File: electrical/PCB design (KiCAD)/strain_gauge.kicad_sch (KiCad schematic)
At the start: 12 parts, among them U6 INA125U

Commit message: documentation update for my 10 days leave ; documentation for first time teensy setup on Arduino IDE ;  SW revamp to use HW versioning conditional compiling
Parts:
- added R19, R23: 1M, Resistor_THT:R_Axial_DIN0207_L6.3mm_D2.5mm_P10.16mm_Horizontal, symbol TMotor_Rev0_5_1_Mark_2_NAU_OpenExo-eagle-import:R-US_0207/10
- R16: value 470R -> 10R
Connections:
- net GND: now also R19.2, R23.2
- net Vbridge+: now also R19.1
- net Vbridge-: now also R23.1
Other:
- note added: "weak pull down to avoid saturating output amplifier"

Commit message: design updates ; documentation update
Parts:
- removed C19: 100nF, Capacitor_THT:C_Disc_D10.5mm_W5.0mm_P5.00mm, symbol TMotor_Rev0_5_1_Mark_2_NAU_OpenExo-eagle-import:C-EU050-024X044
- removed D1: BAT54S, Package_TO_SOT_SMD:SOT-23, symbol Diode:BAT54S
- removed INA_EXC_JP6: SolderJumper_3_Open, Jumper:SolderJumper-3_P1.3mm_Open_RoundedPad1.0x1.5mm_NumberLabels, symbol Jumper:SolderJumper_3_Open
- added C32, C36: 10nF, Capacitor_SMD:C_0805_2012Metric_Pad1.18x1.45mm_HandSolder, symbol TMotor_Rev0_5_1_Mark_2_NAU_OpenExo-eagle-import:C-EU050-024X044
- added D7: BAS70-04, BAS70-04:P200_SOT-23, symbol BAS70-04:BAS70-04
- added INA_EXC_JP2: SolderJumper_2_Open, Jumper:SolderJumper-2_P1.3mm_Open_RoundedPad1.0x1.5mm, symbol Jumper:SolderJumper_2_Open
- added R22: 1k, Resistor_SMD:R_0805_2012Metric_Pad1.20x1.40mm_HandSolder, symbol Device:R
- C13: renamed from C10; footprint (none) -> Capacitor_SMD:C_0805_2012Metric_Pad1.18x1.45mm_HandSolder
- C14: renamed from C24; footprint Capacitor_THT:C_Disc_D10.5mm_W5.0mm_P5.00mm -> Capacitor_SMD:C_0805_2012Metric_Pad1.18x1.45mm_HandSolder
- C15: renamed from C14; footprint (none) -> Capacitor_SMD:C_0805_2012Metric_Pad1.18x1.45mm_HandSolder
- C16: renamed from C25; footprint Capacitor_THT:C_Disc_D10.5mm_W5.0mm_P5.00mm -> Capacitor_SMD:C_0805_2012Metric_Pad1.18x1.45mm_HandSolder
- R6: renamed from R3; value 4.7k -> 1k; footprint Resistor_THT:R_Axial_DIN0207_L6.3mm_D2.5mm_P10.16mm_Horizontal -> Resistor_SMD:R_0805_2012Metric_Pad1.20x1.40mm_HandSolder
- R7: renamed from R16; value 10R -> 50; footprint Resistor_THT:R_Axial_DIN0207_L6.3mm_D2.5mm_P10.16mm_Horizontal -> Resistor_SMD:R_0805_2012Metric_Pad1.20x1.40mm_HandSolder
- R8: renamed from R19; value 1M -> 100k; footprint Resistor_THT:R_Axial_DIN0207_L6.3mm_D2.5mm_P10.16mm_Horizontal -> Resistor_SMD:R_0805_2012Metric_Pad1.20x1.40mm_HandSolder
- R9: renamed from R23; value 1M -> 100k; footprint Resistor_THT:R_Axial_DIN0207_L6.3mm_D2.5mm_P10.16mm_Horizontal -> Resistor_SMD:R_0805_2012Metric_Pad1.20x1.40mm_HandSolder
- renumbered INA_PWR_JP6 to INA_PWR_JP2, INA_VREF_JP6 to INA_VREF_JP2, U6 to U2
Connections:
- net +3V3: now also D7.2 (C)
- net GND: now also C32.1, C36.1, D7.1 (A)
- net Vamplified: now also C32.2, D7.3
- net Vexcitation+: now also C36.2, R22.2
- net at INA_VREF_JP2.2 (C), U2.4 (VREFOUT), U2.5 (IAREF): now also INA_EXC_JP2.1 (A)
- new net: INA_EXC_JP2.2 (B), R22.1
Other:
- note added: "ADC kickback filter for Nano's sample and hold current transients"
- moved on the sheet: R9

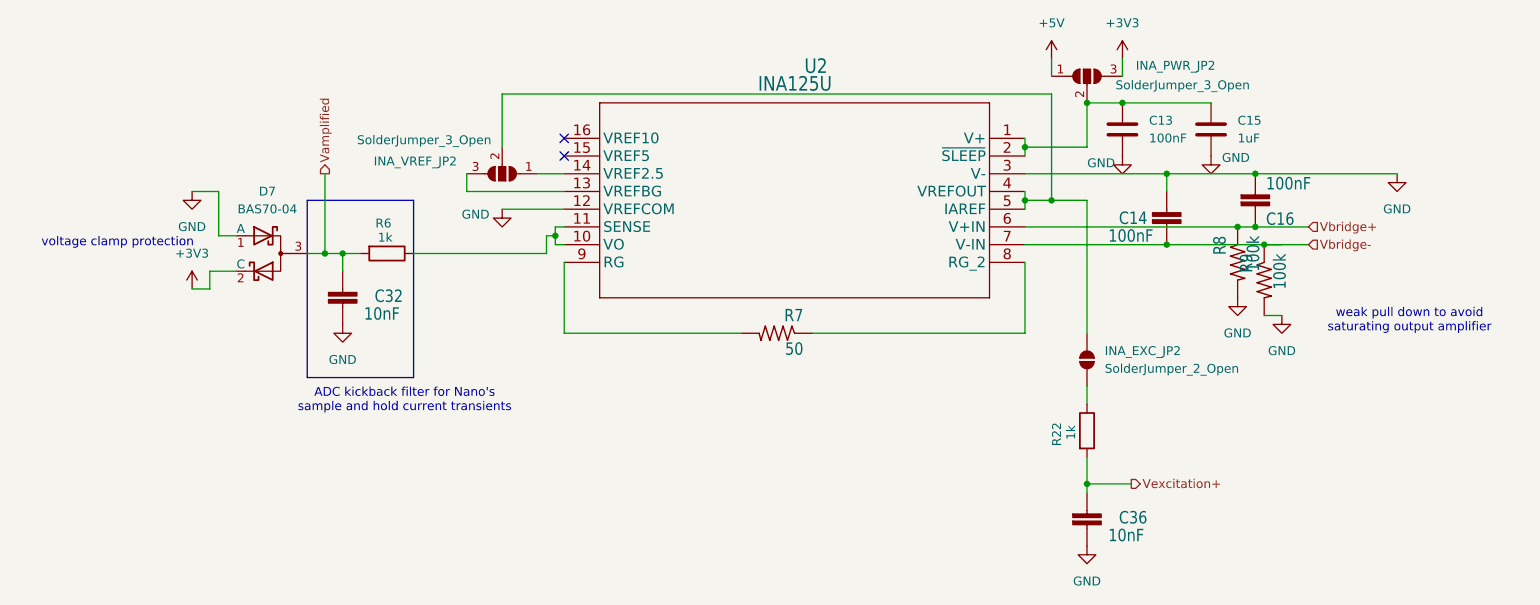
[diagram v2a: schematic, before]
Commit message: updated ble and uart
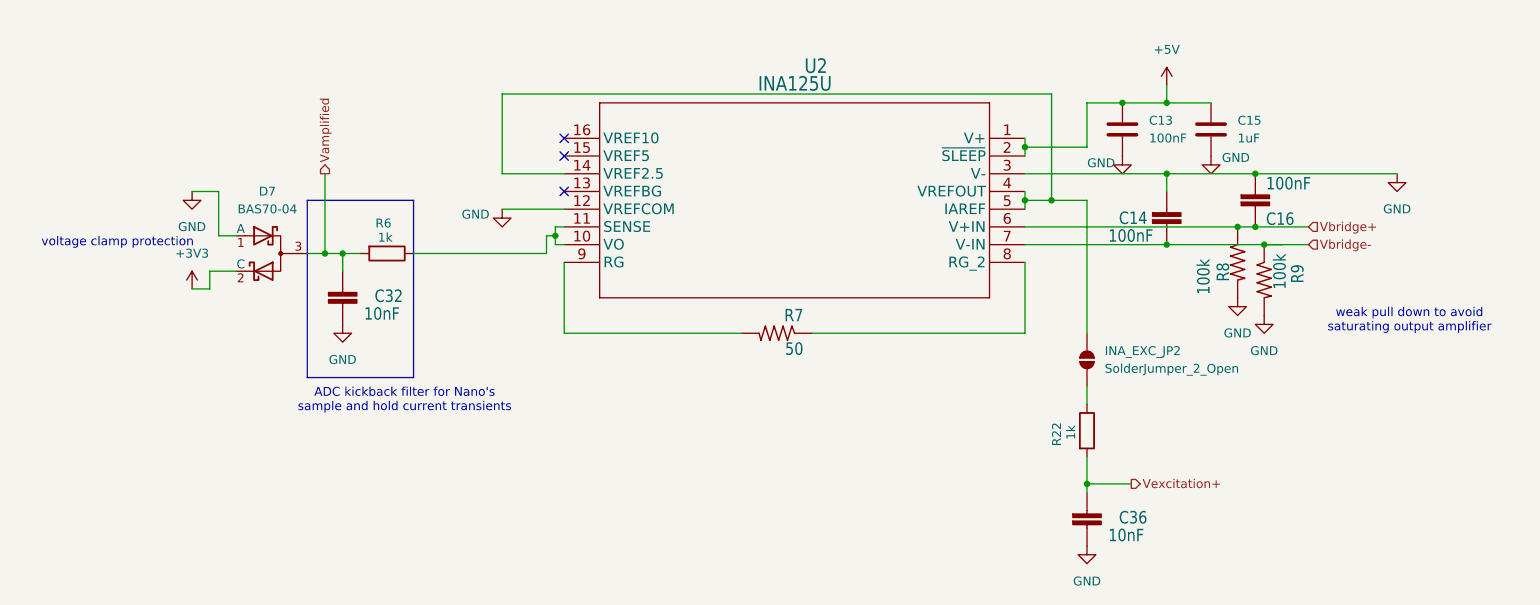
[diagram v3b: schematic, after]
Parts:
- removed INA_PWR_JP2, INA_VREF_JP2: SolderJumper_3_Open, Jumper:SolderJumper-3_P1.3mm_Open_RoundedPad1.0x1.5mm_NumberLabels, symbol Jumper:SolderJumper_3_Open
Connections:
- net +5V: now also C13.1, C15.1, U2.1 (V+), U2.2 (~{SLEEP})
- net at INA_EXC_JP2.1 (A), U2.4 (VREFOUT), U2.5 (IAREF): now also U2.14 (VREF2.5)
- no-connect marks 2 -> 3
